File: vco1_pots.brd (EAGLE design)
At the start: 106 x 50 mm, 30 parts

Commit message: Massive Changes, See Readme
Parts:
- removed U$1: (no value), MusicThingModular:MOUNTING_HOLE
- added JP2, JP3: (no value), pinhead:1_05X2MM
- 1V/OCT, EXP_FM, LINEAR_FM, PULSE_OUT, PWM_INPUT, SINE_OUT, TRIANGLE_OUT: value THONKICONNNEW -> WQP-PJ301M-12_JACK_LOW_SPACE; device MusicThingModular:WQP-PJ301M-12_JACK -> thonkiconn:WQP-PJ301M-12_JACK_LOW_SPACE
- moved 1V/OCT 45.3 mm to (6.50, 34.8)
- moved EXP_FM 44.8 mm to (18.8, 15.2)
- moved LINEAR_FM 37.3 mm to (18.8, 5.39)
- moved PWM_CV 35.7 mm to (52.2, 41.7)
- moved R35 30.8 mm to (50.2, 21.6), turned to 180 degrees
- moved PWM_INPUT 27.8 mm to (6.50, 44.7)
- moved R34 26.9 mm to (39.4, 12.7), turned to 270 degrees
- moved FM_LEVEL 25.9 mm to (33.6, 28.4)
- moved R5 23.8 mm to (55.2, 26.7), turned to 180 degrees
- moved C2 23.5 mm to (31.8, 10.2), turned to 180 degrees
- moved LIN_FM_LEVEL1 22.9 mm to (52.1, 13.2)
- moved R6 12.1 mm to (55.2, 24.1)
- moved R33 11.4 mm to (20.3, 27.3)
- moved R3 11.3 mm to (45.1, 6.35)
- moved R14 10.2 mm to (30.5, 15.2)
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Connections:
- net GND: now also 1V/OCT.P$3, EXP_FM.P$3, JP2.1, JP2.2, JP2.3, JP2.4, JP2.5, JP3.1, JP3.2, JP3.3, JP3.4, JP3.5, LINEAR_FM.P$3, PULSE_OUT.P$3, PWM_INPUT.P$3, SINE_OUT.P$3, TRIANGLE_OUT.P$3; no longer 1V/OCT.P$3_SLEEVE, EXP_FM.P$3_SLEEVE, LINEAR_FM.P$3_SLEEVE, PULSE_OUT.P$3_SLEEVE, PWM_INPUT.P$3_SLEEVE, SINE_OUT.P$3_SLEEVE, TRIANGLE_OUT.P$3_SLEEVE
- net N$1: now also 1V/OCT.P$1; no longer 1V/OCT.P$1_TIP
- net N$18: now also TRIANGLE_OUT.P$1; no longer TRIANGLE_OUT.P$1_TIP
- net N$2: now also EXP_FM.P$1; no longer EXP_FM.P$1_TIP
- net N$20: now also LINEAR_FM.P$1; no longer LINEAR_FM.P$1_TIP
- net N$37: now also SINE_OUT.P$1; no longer SINE_OUT.P$1_TIP
- net N$41: now also PULSE_OUT.P$1; no longer PULSE_OUT.P$1_TIP
- net N$42: now also PWM_INPUT.P$1; no longer PWM_INPUT.P$1_TIP
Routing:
- net N$44: track 60.0 -> 22.1 mm
- net N$4: track 67.3 -> 32.4 mm
- net N$42: track 22.5 -> 45.4 mm
- net PWM_CV: track 45.3 -> 25.0 mm
- net +12V: track 93.7 -> 75.9 mm
- net N$17: track 23.0 -> 8.93 mm
- net N$20: track 3.89 -> 16.4 mm
- net N$2: track 30.0 -> 17.7 mm
- net N$1: track 29.3 -> 41.3 mm
- net N$43: track 15.8 -> 27.1 mm
- net N$41: track 28.7 -> 18.1 mm
- net N$19: track 21.4 -> 10.9 mm
- net N$37: track 17.5 -> 27.3 mm
- net CV_A: track 40.8 -> 32.4 mm
- net N$18: track 18.8 -> 27.0 mm
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
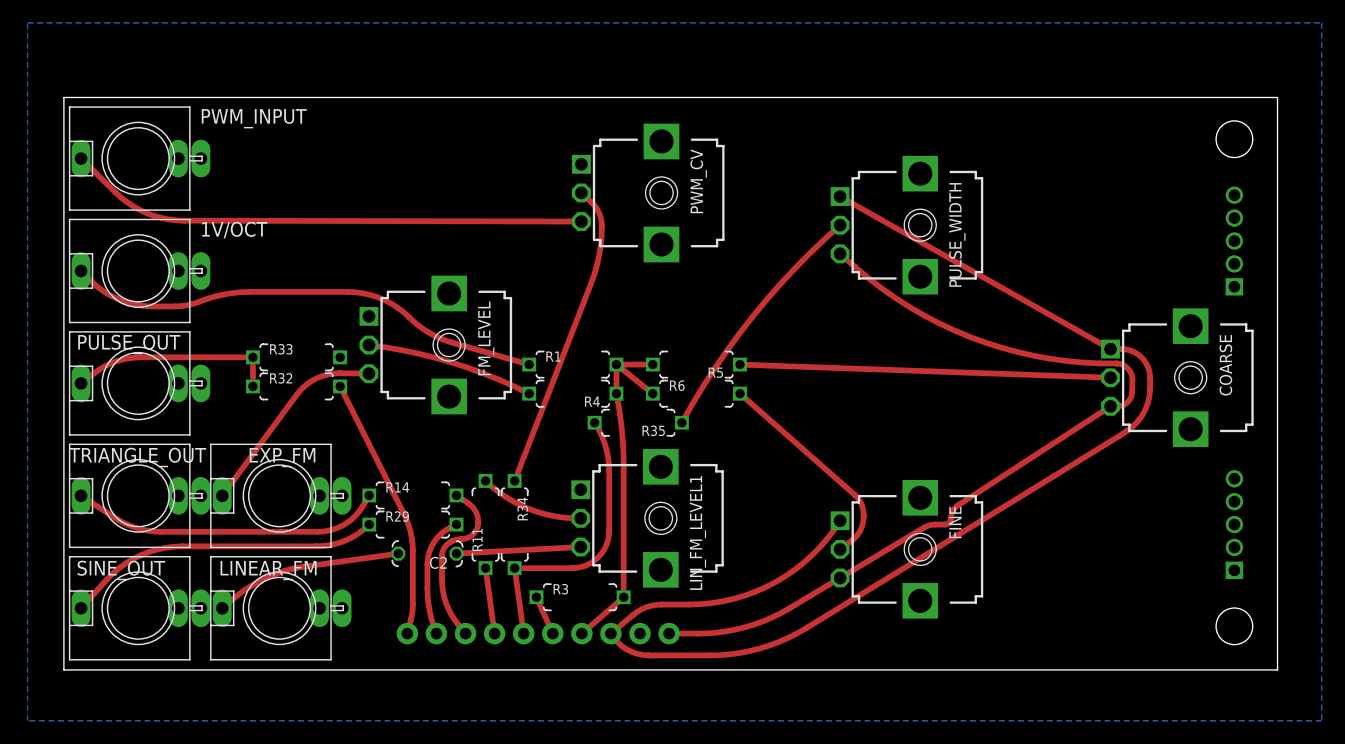
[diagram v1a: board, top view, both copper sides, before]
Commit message: Changed PCB Size, Moved Frequency Knob
Adapted PCB Boards for the (cheaper) size of 100x49mm which allows two
PCBs on one 100x100mm Panel. Frequency Pot had to be moved X -1mm
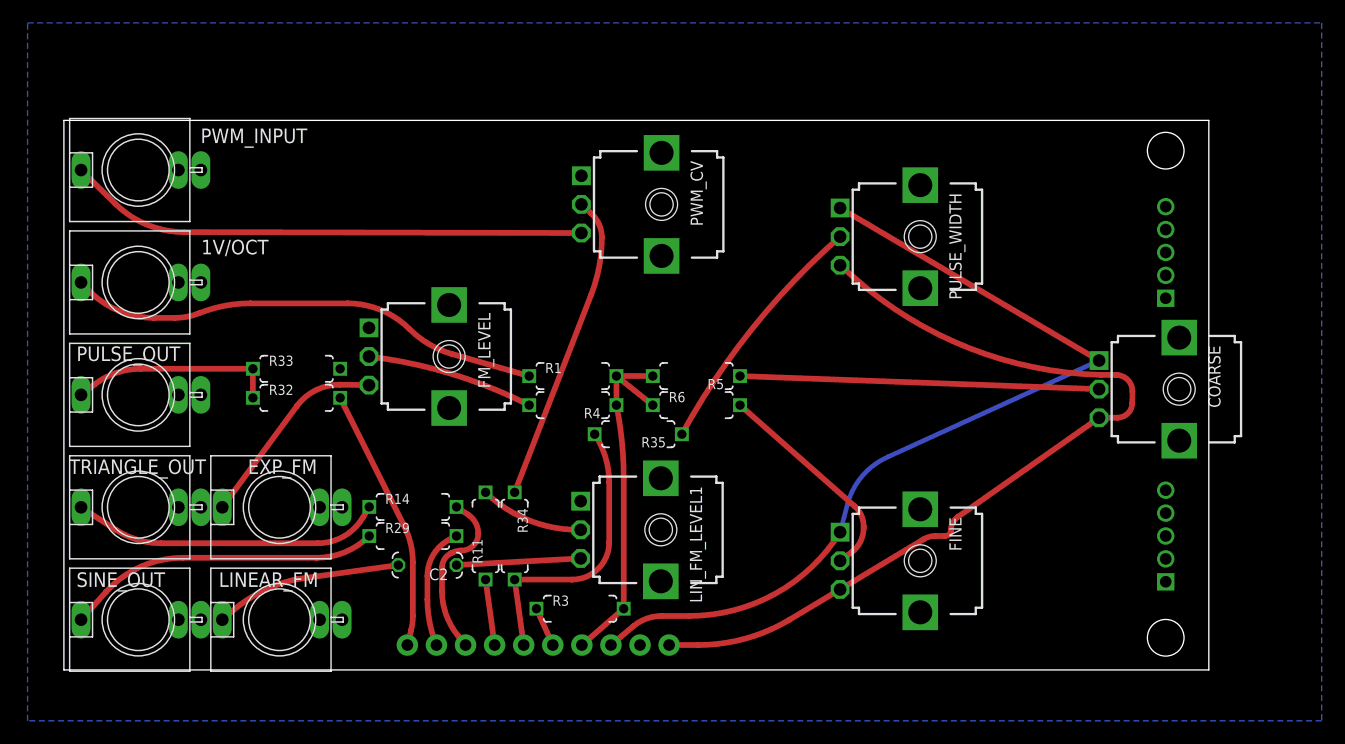
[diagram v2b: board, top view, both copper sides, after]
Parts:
- moved JP2 6.08 mm to (96.2, 11.7)
- moved JP3 6.08 mm to (96.2, 36.5)
- moved U$2 6.08 mm to (96.2, 2.81)
- moved U$3 6.08 mm to (96.2, 45.4)
- moved COARSE 1.41 mm to (97.4, 24.5)
- moved 1V/OCT 1.00 mm to (6.50, 33.8)
- moved C2 1.00 mm to (31.8, 9.16)
- moved EXP_FM 1.00 mm to (18.8, 14.2)
- moved FINE 1.00 mm to (74.8, 9.53)
- moved FM_LEVEL 1.00 mm to (33.6, 27.4)
- moved JP1 1.00 mm to (30.0, 2.17)
- moved LINEAR_FM 1.00 mm to (18.8, 4.39)
- moved LIN_FM_LEVEL1 1.00 mm to (52.1, 12.2)
- moved PULSE_OUT 1.00 mm to (6.50, 24.0)
- moved PULSE_WIDTH 1.00 mm to (74.8, 37.8)
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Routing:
- net -12V: track 110.2 -> 77.1 mm
- net N$4: track 32.4 -> 31.4 mm
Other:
- board size 106 x 50 mm -> 100 x 48 mm

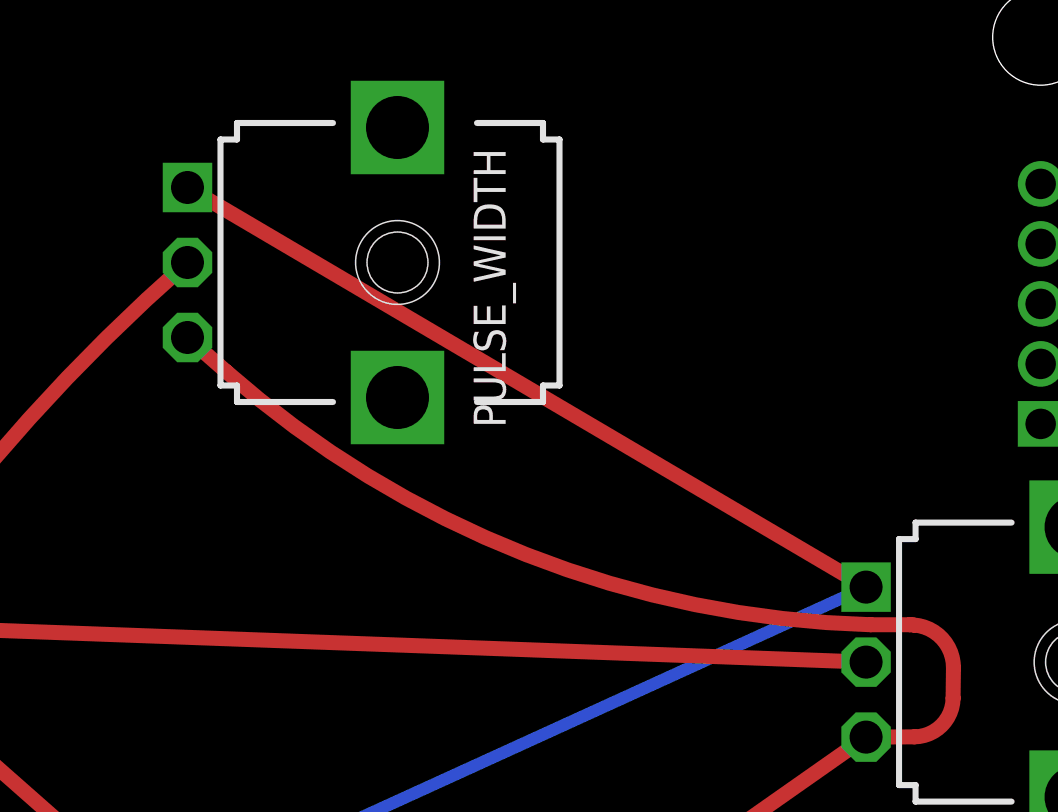
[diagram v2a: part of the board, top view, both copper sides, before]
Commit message: Fixed small Clearance Problems
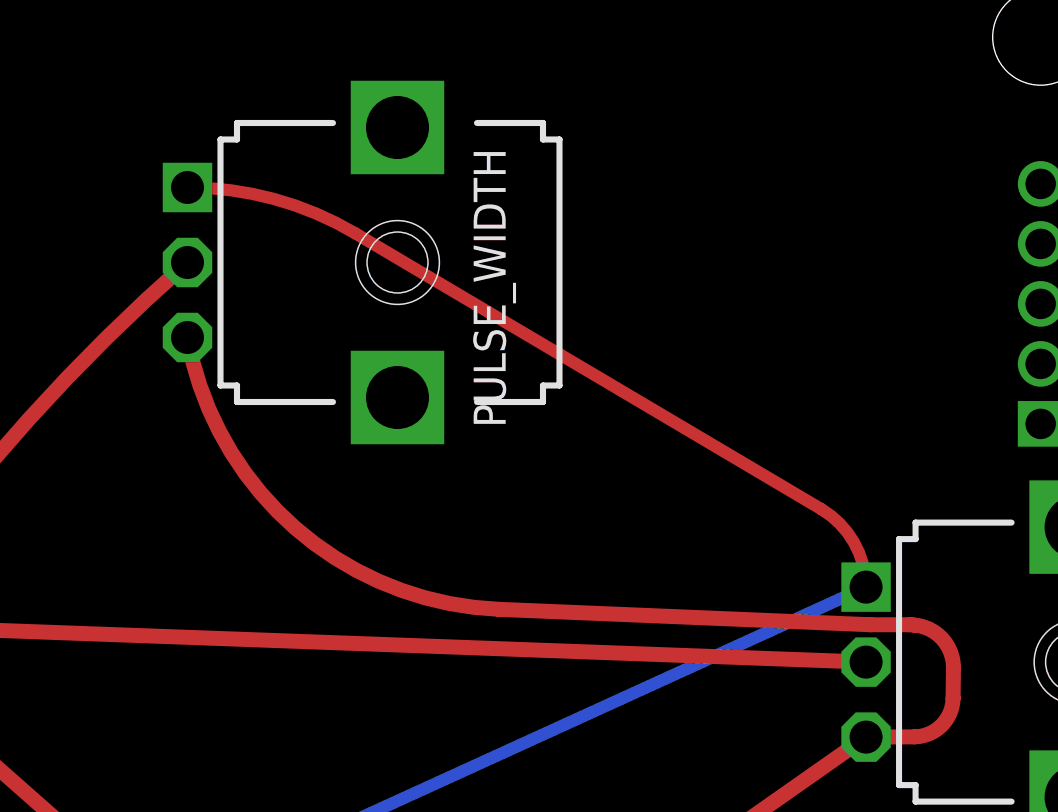
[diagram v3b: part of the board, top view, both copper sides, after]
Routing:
- net +12V: track 76.1 -> 77.5 mm
- net -12V: track 77.1 -> 77.7 mm
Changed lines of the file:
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@@
 <layers>
 <layer number="1" name="Top" color="4" fill="1" visible="yes" active="yes"/>
-<layer number="2" name="Route2" color="1" fill="3" visible="yes" active="yes"/>
+<layer number="2" name="Route2" color="1" fill="3" visible="no" active="no"/>
 <layer number="3" name="Route3" color="4" fill="3" visible="no" active="no"/>
 <layer number="4" name="Route4" color="1" fill="4" visible="no" active="no"/>
@@
 <layer number="13" name="Route13" color="4" fill="5" visible="no" active="no"/>
 <layer number="14" name="Route14" color="1" fill="6" visible="no" active="no"/>
-<layer number="15" name="Route15" color="4" fill="6" visible="no" active="yes"/>
+<layer number="15" name="Route15" color="4" fill="6" visible="no" active="no"/>
 <layer number="16" name="Bottom" color="1" fill="1" visible="yes" active="yes"/>
 <layer number="17" name="Pads" color="2" fill="1" visible="yes" active="yes"/>
@@
 </class>
 </classes>
-<designrules name="SeeedStudio_DRU_no_angle_20130527">
+<designrules name="Elecrow_2-layer_PCB_eagle_rule">
 <description language="de">&lt;b&gt;EAGLE Design Rules&lt;/b&gt;
 &lt;p&gt;
@@
 necessary adjustments and save your customized
 design rules under a new name.</description>
-<description language="zh">&lt;b&gt;Seeed Studio EAGLE Design Rules&lt;/b&gt;
+<description language="zh">&lt;b&gt;Elecrow PCB EAGLE Design Rules&lt;/b&gt;
 </description>
-<param name="layerSetup" value="(1*2*15*16)"/>
-<param name="mtCopper" value="0.035mm 0.0175mm 0.035mm 0.035mm 0.035mm 0.035mm 0.035mm 0.035mm 0.035mm 0.035mm 0.035mm 0.035mm 0.035mm 0.035mm 0.0175mm 0.035mm"/>
-<param name="mtIsolate" value="0.2mm 1.1mm 0.2mm 0.15mm 0.2mm 0.15mm 0.2mm 0.15mm 0.2mm 0.15mm 0.2mm 0.15mm 0.2mm 0.15mm 0.2mm"/>
+<param name="layerSetup" value="(1*16)"/>
+<param name="mtCopper" value="0.035mm 0.035mm 0.035mm 0.035mm 0.035mm 0.035mm 0.035mm 0.035mm 0.035mm 0.035mm 0.035mm 0.035mm 0.035mm 0.035mm 0.035mm 0.035mm"/>
+<param name="mtIsolate" value="1.6mm 1.2mm 0.2mm 0.15mm 0.2mm 0.15mm 0.2mm 0.15mm 0.2mm 0.15mm 0.2mm 0.15mm 0.2mm 0.15mm 0.2mm"/>
 <param name="mdWireWire" value="6mil"/>
 <param name="mdWirePad" value="6mil"/>
@@
 <param name="mdPadPad" value="6mil"/>
 <param name="mdPadVia" value="6mil"/>
-<param name="mdViaVia" value="6mil"/>
+<param name="mdViaVia" value="8mil"/>
 <param name="mdSmdPad" value="0mil"/>
 <param name="mdSmdVia" value="0mil"/>
@@
 <param name="mdViaViaSameLayer" value="8mil"/>
 <param name="mnLayersViaInSmd" value="2"/>
-<param name="mdCopperDimension" value="10mil"/>
+<param name="mdCopperDimension" value="20mil"/>
 <param name="mdDrill" value="10mil"/>
 <param name="mdSmdStop" value="0mil"/>
@@
 <param name="mvStopFrame" value="1"/>
 <param name="mvCreamFrame" value="0"/>
-<param name="mlMinStopFrame" value="2mil"/>
-<param name="mlMaxStopFrame" value="2mil"/>
+<param name="mlMinStopFrame" value="0mil"/>
+<param name="mlMaxStopFrame" value="0mil"/>
 <param name="mlMinCreamFrame" value="0mil"/>
 <param name="mlMaxCreamFrame" value="0mil"/>
-<param name="mlViaStopLimit" value="25mil"/>
+<param name="mlViaStopLimit" value="100mil"/>
 <param name="srRoundness" value="0"/>
 <param name="srMinRoundness" value="0mil"/>
@@
 <wire x1="55.38315" y1="2.175" x2="63.38441875" y2="4.38864375" width="0.5" layer="1" curve="30.929437"/>
 <wire x1="63.38441875" y1="4.38864375" x2="67.796" y2="7.032" width="0.5" layer="1"/>
-<wire x1="67.796" y1="35.345" x2="69.070109375" y2="34.22314375" width="0.5" layer="1"/>
-<wire x1="69.070109375" y1="34.22314375" x2="90.57" y2="25.77" width="0.5" layer="1" curve="39.80137"/>
 <wire x1="90.57" y1="25.77" x2="91.87765" y2="25.77" width="0.5" layer="1"/>
 <wire x1="90.415" y1="22.025" x2="78.116628125" y2="13.389878125" width="0.5" layer="1"/>
@@
 <wire x1="93.315790625" y1="23.32026875" x2="92.029853125" y2="22.033153125" width="0.5" layer="1" curve="-88.528005"/>
 <wire x1="92.029853125" y1="22.033153125" x2="90.415" y2="22.025" width="0.5" layer="1"/>
+<wire x1="90.57" y1="25.77" x2="78.175190625" y2="26.284015625" width="0.5" layer="1"/>
+<wire x1="78.175190625" y1="26.284015625" x2="67.796" y2="35.345" width="0.5" layer="1" curve="-77.492299"/>
 </signal>
 <signal name="-12V">
@@
 <contactref element="PULSE_WIDTH" pad="1"/>
 <contactref element="JP1" pad="8"/>
-<wire x1="67.796" y1="40.345" x2="90.415" y2="27.025" width="0.5" layer="1"/>
 <wire x1="54.61" y1="4.715" x2="52.20836875" y2="4.715" width="0.5" layer="1"/>
 <wire x1="52.20836875" y1="4.715" x2="49.72216875" y2="3.808478125" width="0.5" layer="1" curve="40.065853"/>
@@
 <wire x1="72.003453125" y1="18.622075" x2="68.440484375" y2="14.4768625" width="0.4064" layer="16" curve="51.825444"/>
 <wire x1="68.440484375" y1="14.4768625" x2="67.796" y2="12.032" width="0.4064" layer="16"/>
+<wire x1="67.796" y1="40.345" x2="73.385175" y2="38.82" width="0.4064" layer="1" curve="-30.713172"/>
+<wire x1="73.385175" y1="38.82" x2="88.91545" y2="29.6286125" width="0.4064" layer="1"/>
+<wire x1="88.91545" y1="29.6286125" x2="90.415" y2="27.025" width="0.4064" layer="1" curve="-58.883238"/>
 </signal>
 <signal name="N$4">
